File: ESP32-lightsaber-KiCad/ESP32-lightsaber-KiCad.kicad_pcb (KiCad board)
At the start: 2 copper layers, 7 parts, among them J1 Conn_01x05, SW1 SW_Push

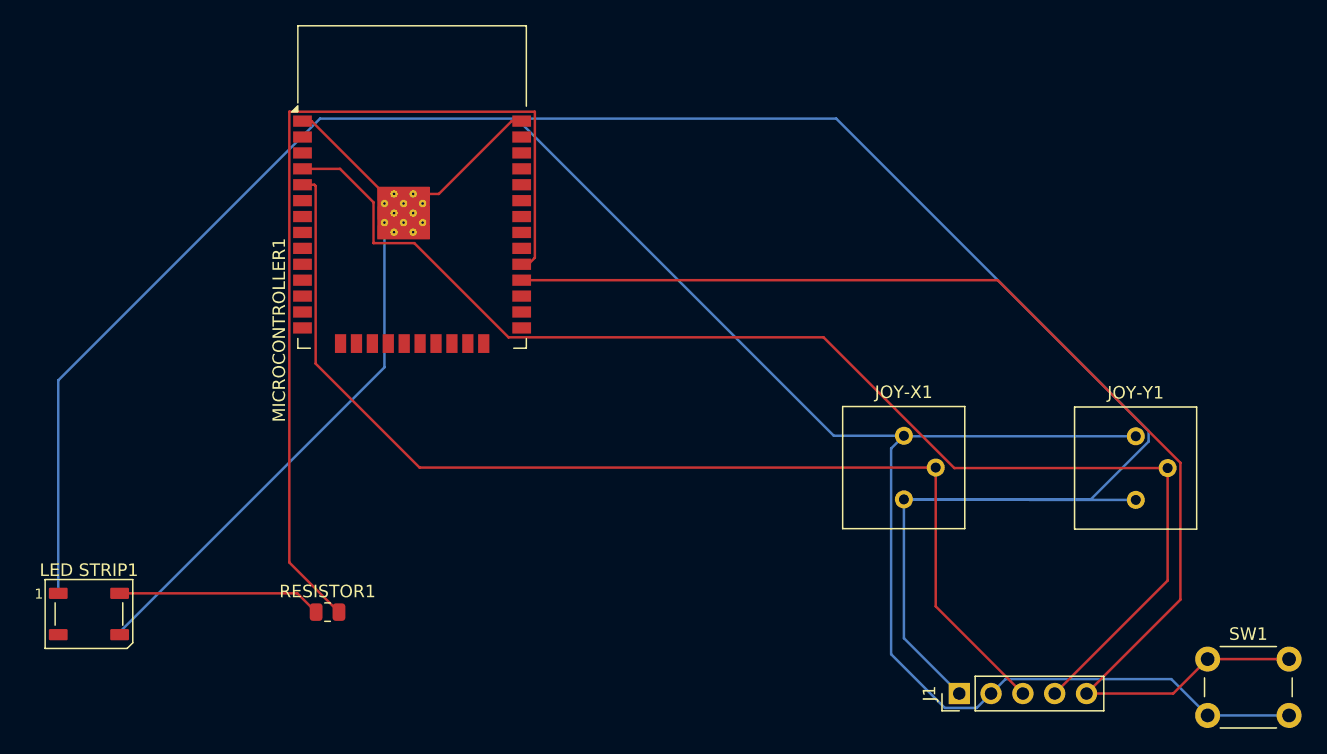
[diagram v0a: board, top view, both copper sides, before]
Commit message: Modified lightsaber schematic & PCB following prototype feedback
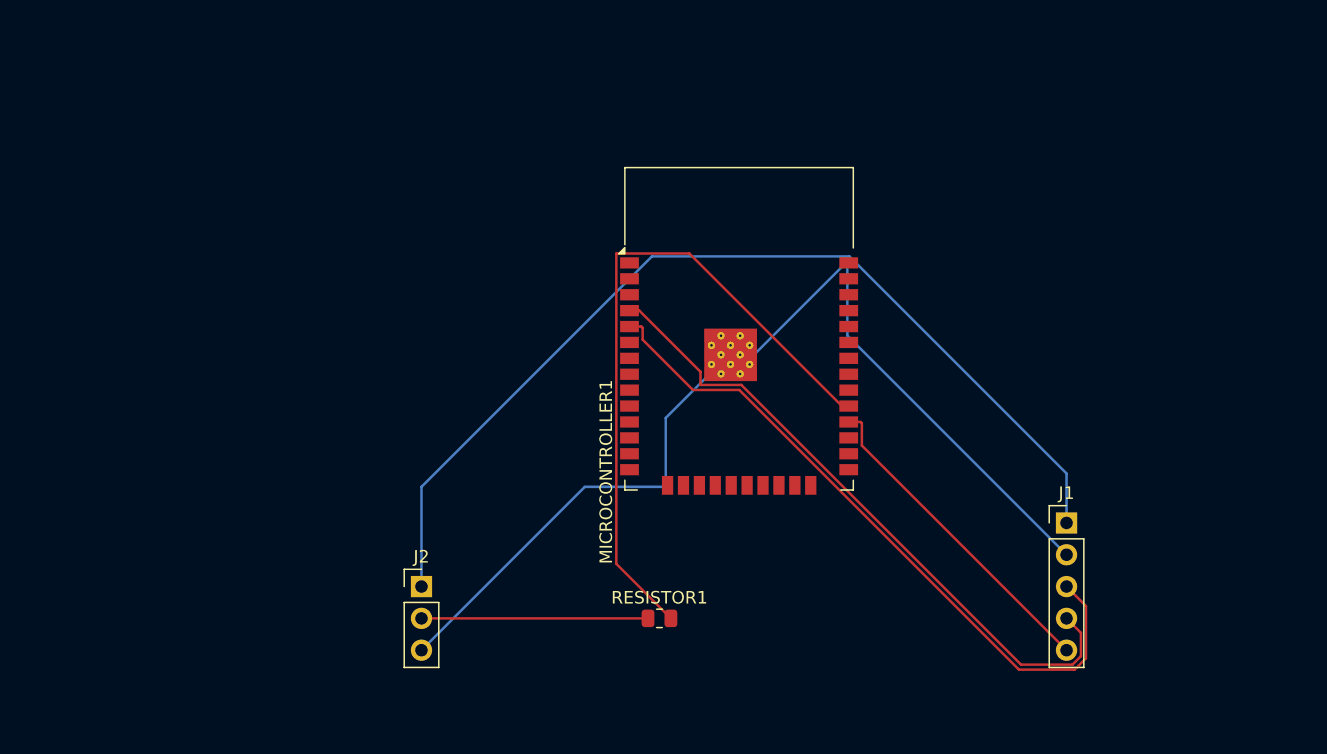
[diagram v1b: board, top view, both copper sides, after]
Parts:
- removed JOY-X1, JOY-Y1: R_Potentiometer, Potentiometer_THT:Potentiometer_Bourns_3386P_Vertical
- removed LED STRIP1: WS2812B, LED_SMD:LED_WS2812B_PLCC4_5.0x5.0mm_P3.2mm
- removed SW1: SW_Push, Button_Switch_THT:SW_PUSH_6mm_H9.5mm
- added J2: Conn_01x03, Connector_PinHeader_2.54mm:PinHeader_1x03_P2.54mm_Vertical, F.Cu at (95.0, 111.0)
- moved MICROCONTROLLER1 28.5 mm to (120.4, 93.4)
- moved RESISTOR1 26.5 mm to (114.0, 113.5)
- moved J1 16.1 mm to (146.5, 105.9), turned to 0 degrees
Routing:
- net +5V: track 181.2 -> 78.2 mm
- net GND: track 174.0 -> 80.7 mm
- net Net-(J1-Pin_5): track 97.5 -> 26.0 mm
- net Net-(J1-Pin_4): track 102.6 -> 52.1 mm
- net Net-(J1-Pin_3): track 89.1 -> 55.1 mm
- net Net-(MICROCONTROLLER1-IO5): track 74.1 -> 54.5 mm
- net Net-(J2-Pin_2): track 16.3 -> 18.1 mm

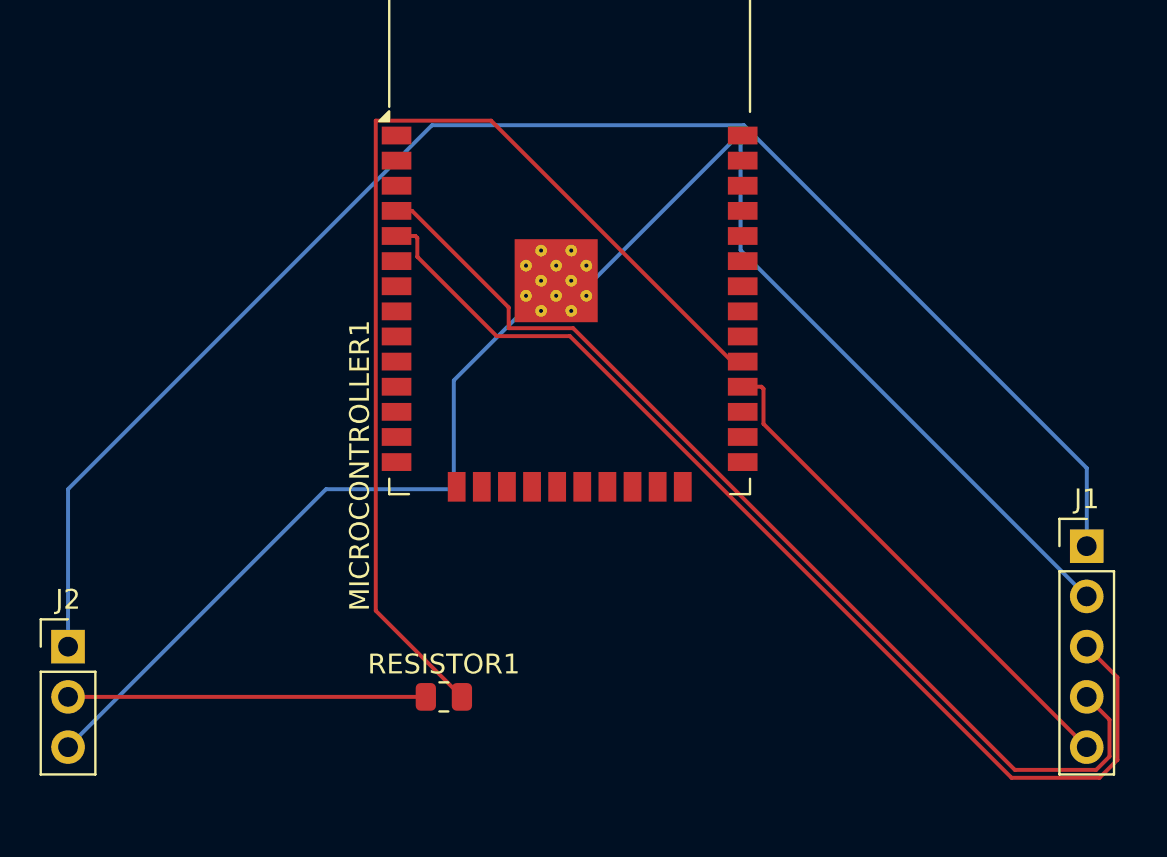
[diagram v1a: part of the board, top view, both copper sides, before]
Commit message: Thickened wires for 5V+ power & GND in PCB prototype for current flow
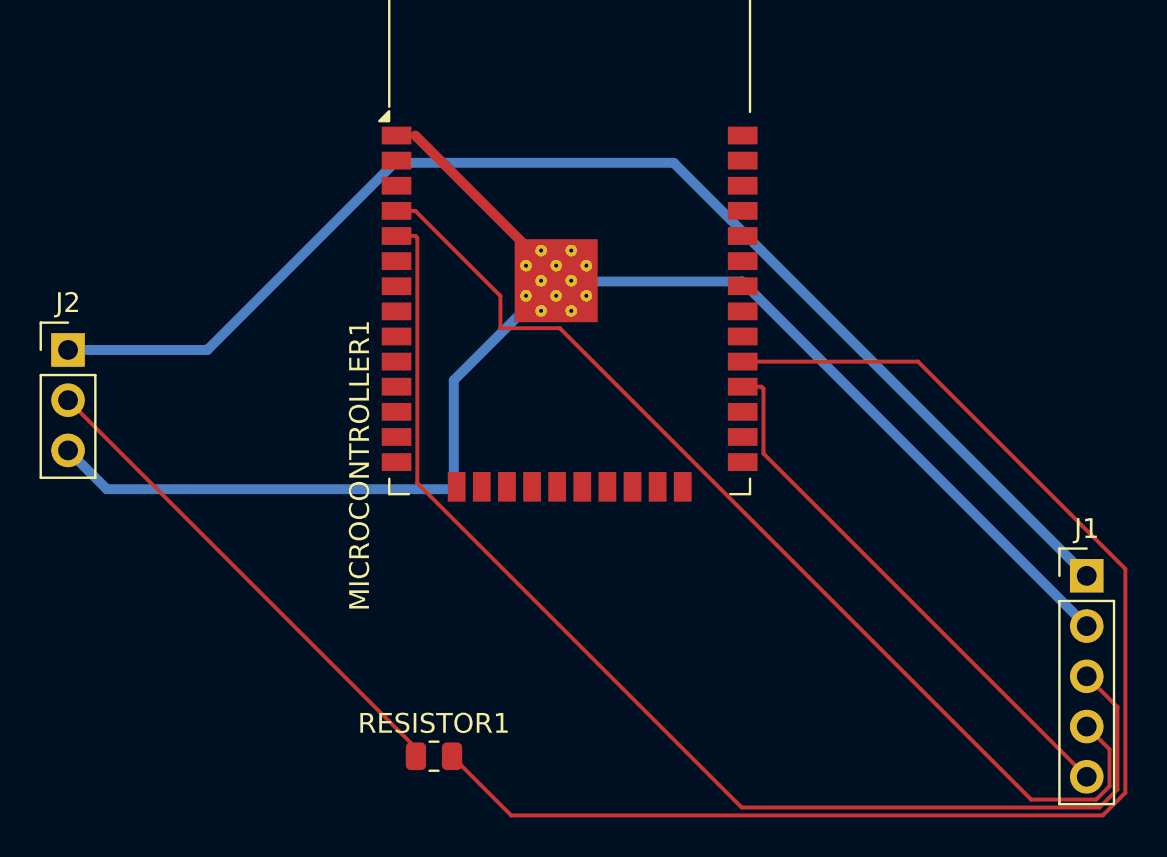
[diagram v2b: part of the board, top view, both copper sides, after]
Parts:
- moved J2 15.0 mm to (95.0, 96.0)
- moved RESISTOR1 3.04 mm to (113.5, 116.5)
- moved J1 1.50 mm to (146.5, 107.4)
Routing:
- net Net-(MICROCONTROLLER1-IO5): track 54.5 -> 70.8 mm
- net +5V: track 78.2 -> 64.1 mm
- net Net-(J1-Pin_3): track 55.1 -> 62.4 mm
- net Net-(J2-Pin_2): track 18.1 -> 25.3 mm
- net GND: track 80.7 -> 78.3 mm
- net Net-(J1-Pin_5): track 26.0 -> 27.5 mm
- net Net-(J1-Pin_4): track 52.1 -> 53.1 mm
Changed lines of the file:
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@@
 	(footprint "Connector_PinHeader_2.54mm:PinHeader_1x03_P2.54mm_Vertical"
 		(layer "F.Cu")
-		(at 95 110.96)
+		(at 95 95.96)
 		(descr "Through hole straight pin header, 1x03, 2.54mm pitch, single row")
 		(tags "Through hole pin header THT 1x03 2.54mm single row")
@@
 	(footprint "Resistor_SMD:R_0805_2012Metric"
 		(layer "F.Cu")
-		(at 114 113.5)
+		(at 113.5 116.5)
 		(descr "Resistor SMD 0805 (2012 Metric), square (rectangular) end terminal, IPC-7351 nominal, (Body size source: IPC-SM-782 page 72, https://www.pcb-3d.com/wordpress/wp-content/uploads/ipc-sm-782a_amendment_1_and_2.pdf), generated with kicad-footprint-generator")
 		(tags "resistor")
@@
 	(footprint "Connector_PinHeader_2.54mm:PinHeader_1x05_P2.54mm_Vertical"
 		(layer "F.Cu")
-		(at 146.5 105.88)
+		(at 146.5 107.38)
 		(descr "Through hole straight pin header, 1x05, 2.54mm pitch, single row")
 		(tags "Through hole pin header THT 1x05 2.54mm single row")
@@
 	)
 	(segment
-		(start 129 90.92)
-		(end 129 85)
-		(width 0.2)
+		(start 119.6775 92.24)
+		(end 119.6775 92.46)
+		(width 0.2)
+		(layer "F.Cu")
+		(net 1)
+	)
+	(segment
+		(start 111.6075 85.12)
+		(end 112.5575 85.12)
+		(width 0.2)
+		(layer "F.Cu")
+		(net 1)
+	)
+	(segment
+		(start 112.5575 85.12)
+		(end 119.6775 92.24)
+		(width 0.5)
+		(layer "F.Cu")
+		(net 1)
+	)
+	(segment
+		(start 96.96 103)
+		(end 95 101.04)
+		(width 0.5)
 		(layer "B.Cu")
 		(net 1)
 	)
 	(segment
-		(start 146.5 108.42)
-		(end 129 90.92)
-		(width 0.2)
+		(start 119.5 92.5)
+		(end 114.5 97.5)
+		(width 0.5)
 		(layer "B.Cu")
 		(net 1)
@@
 	(segment
 		(start 114.5 103)
-		(end 108.04 103)
-		(width 0.2)
+		(end 96.96 103)
+		(width 0.5)
 		(layer "B.Cu")
 		(net 1)
 	)
 	(segment
-		(start 129 85)
-		(end 121.5 92.5)
-		(width 0.2)
+		(start 129.08 92.5)
+		(end 119.5 92.5)
+		(width 0.5)
 		(layer "B.Cu")
 		(net 1)
 	)
 	(segment
-		(start 119.5 92.5)
-		(end 114.5 97.5)
-		(width 0.2)
+		(start 146.5 109.92)
+		(end 129.08 92.5)
+		(width 0.5)
 		(layer "B.Cu")
 		(net 1)
 	)
 	(segment
-		(start 108.04 103)
-		(end 95 116.04)
-		(width 0.2)
+		(start 114.5 97.5)
+		(end 114.5 103)
+		(width 0.5)
 		(layer "B.Cu")
 		(net 1)
 	)
 	(segment
-		(start 114.5 97.5)
-		(end 114.5 103)
-		(width 0.2)
-		(layer "B.Cu")
-		(net 1)
-	)
-	(segment
-		(start 121.5 92.5)
-		(end 119.5 92.5)
-		(width 0.2)
-		(layer "B.Cu")
-		(net 1)
-	)
-	(segment
-		(start 146.5 101.9329)
-		(end 146.5 105.88)
-		(width 0.2)
+		(start 111.5 86.5)
+		(end 125.62 86.5)
+		(width 0.5)
 		(layer "B.Cu")
 		(net 2)
 	)
 	(segment
-		(start 95 110.96)
-		(end 95 103)
-		(width 0.2)
+		(start 95 95.96)
+		(end 102.04 95.96)
+		(width 0.5)
 		(layer "B.Cu")
 		(net 2)
 	)
 	(segment
-		(start 113.401 84.599)
-		(end 129.1661 84.599)
-		(width 0.2)
+		(start 102.04 95.96)
+		(end 111.5 86.5)
+		(width 0.5)
 		(layer "B.Cu")
 		(net 2)
 	)
 	(segment
-		(start 95 103)
-		(end 113.401 84.599)
-		(width 0.2)
+		(start 125.62 86.5)
+		(end 146.5 107.38)
+		(width 0.5)
 		(layer "B.Cu")
 		(net 2)
 	)
 	(segment
-		(start 129.1661 84.599)
-		(end 146.5 101.9329)
-		(width 0.2)
-		(layer "B.Cu")
-		(net 2)
-	)
-	(segment
-		(start 114.9125 113.5)
-		(end 110.5565 109.144)
+		(start 137.972 96.55)
+		(end 129.1075 96.55)
 		(width 0.2)
 		(layer "F.Cu")
@@
 	)
 	(segment
-		(start 110.5565 84.369)
-		(end 116.3885 84.369)
+		(start 148.453 107.031)
+		(end 137.972 96.55)
 		(width 0.2)
 		(layer "F.Cu")
@@
 	)
 	(segment
-		(start 110.5565 109.144)
-		(end 110.5565 84.369)
+		(start 147.30896 119.493)
+		(end 148.453 118.34896)
 		(width 0.2)
 		(layer "F.Cu")
@@
 	)
 	(segment
-		(start 116.3885 84.369)
-		(end 128.5695 96.55)
+		(start 148.453 118.34896)
+		(end 148.453 107.031)
 		(width 0.2)
 		(layer "F.Cu")
@@
 	)
 	(segment
-		(start 128.5695 96.55)
-		(end 129.1075 96.55)
+		(start 117.4055 119.493)
+		(end 147.30896 119.493)
 		(width 0.2)
 		(layer "F.Cu")
@@
 	)
 	(segment
-		(start 120.5365 94.861)
-		(end 117.2765 94.861)
+		(start 114.4125 116.5)
+		(end 117.4055 119.493)
+		(width 0.2)
+		(layer "F.Cu")
+		(net 16)
+	)
+	(segment
+		(start 112.5575 88.93)
+		(end 111.6075 88.93)
 		(width 0.2)
 		(layer "F.Cu")
@@
 	)
 	(segment
-		(start 147.651 114.651)
-		(end 147.651 116.51676)
+		(start 116.861 93.2335)
+		(end 112.5575 88.93)
 		(width 0.2)
 		(layer "F.Cu")
@@
 	)
 	(segment
-		(start 142.8665 117.191)
-		(end 120.5365 94.861)
+		(start 143.691 118.691)
+		(end 119.861 94.861)
 		(width 0.2)
 		(layer "F.Cu")
@@
 	)
 	(segment
-		(start 112.3925 88.93)
-		(end 111.6075 88.93)
+		(start 147.651 118.01676)
+		(end 146.97676 118.691)
 		(width 0.2)
 		(layer "F.Cu")
@@
 	)
 	(segment
-		(start 146.97676 117.191)
-		(end 142.8665 117.191)
+		(start 119.861 94.861)
+		(end 116.861 94.861)
 		(width 0.2)
 		(layer "F.Cu")
@@
 	)
 	(segment
-		(start 117.2765 94.861)
-		(end 117.2765 93.814)
+		(start 146.5 115)
+		(end 147.651 116.151)
 		(width 0.2)
 		(layer "F.Cu")
@@
 	)
 	(segment
-		(start 117.2765 93.814)
-		(end 112.3925 88.93)
+		(start 146.97676 118.691)
+		(end 143.691 118.691)
 		(width 0.2)
 		(layer "F.Cu")
@@
 	)
 	(segment
-		(start 147.651 116.51676)
-		(end 146.97676 117.191)
+		(start 116.861 94.861)
+		(end 116.861 93.2335)
 		(width 0.2)
 		(layer "F.Cu")
@@
 	)
 	(segment
-		(start 146.5 113.5)
-		(end 147.651 114.651)
+		(start 147.651 116.151)
+		(end 147.651 118.01676)
 		(width 0.2)
 		(layer "F.Cu")
 		(net 26)
-	)
-	(segment
-		(start 146.5 116.04)
-		(end 130.1585 99.6985)
-		(width 0.2)
-		(layer "F.Cu")
-		(net 27)
-	)
-	(segment
-		(start 130.1585 99.6985)
-		(end 130.1585 97.921)
-		(width 0.2)
-		(layer "F.Cu")
-		(net 27)
 	)
 	(segment
@@
 	)
 	(segment
+		(start 146.5 117.54)
+		(end 130.1585 101.1985)
+		(width 0.2)
+		(layer "F.Cu")
+		(net 27)
+	)
+	(segment
+		(start 130.1585 101.1985)
+		(end 130.1585 97.921)
+		(width 0.2)
+		(layer "F.Cu")
+		(net 27)
+	)
+	(segment
 		(start 130.1585 97.921)
 		(end 130.0575 97.82)
@@
 	)
 	(segment
-		(start 116.6695 95.262)
-		(end 112.6585 91.251)
+		(start 129.0575 119.092)
+		(end 112.6585 102.693)
 		(width 0.2)
 		(layer "F.Cu")
@@
 	)
 	(segment
-		(start 142.7004 117.592)
-		(end 120.3704 95.262)
+		(start 112.6585 90.301)
+		(end 112.5575 90.2)
 		(width 0.2)
 		(layer "F.Cu")
@@
 	)
 	(segment
-		(start 148.052 112.512)
-		(end 148.052 116.68286)
+		(start 148.052 118.18286)
+		(end 147.14286 119.092)
 		(width 0.2)
 		(layer "F.Cu")
@@
 	)
 	(segment
-		(start 120.3704 95.262)
-		(end 116.6695 95.262)
-		(width 0.2)
-		(layer "F.Cu")
-		(net 29)
-	)
-	(segment
-		(start 148.052 116.68286)
-		(end 147.14286 117.592)
-		(width 0.2)
-		(layer "F.Cu")
-		(net 29)
-	)
-	(segment
-		(start 112.6585 91.251)
+		(start 112.6585 102.693)
 		(end 112.6585 90.301)
-		(width 0.2)
-		(layer "F.Cu")
-		(net 29)
-	)
-	(segment
-		(start 147.14286 117.592)
-		(end 142.7004 117.592)
-		(width 0.2)
-		(layer "F.Cu")
-		(net 29)
-	)
-	(segment
-		(start 146.5 110.96)
-		(end 148.052 112.512)
 		(width 0.2)
 		(layer "F.Cu")
@@
 	)
 	(segment
-		(start 112.6585 90.301)
-		(end 112.5575 90.2)
+		(start 147.14286 119.092)
+		(end 129.0575 119.092)
 		(width 0.2)
 		(layer "F.Cu")
@@
 	)
 	(segment
-		(start 95 113.5)
-		(end 113.0875 113.5)
-		(width 0.2)
-		(layer "F.Cu")
+		(start 148.052 114.012)
+		(end 148.052 118.18286)
+		(width 0.2)
+		(layer "F.Cu")
+		(net 29)
+	)
+	(segment
+		(start 146.5 112.46)
+		(end 148.052 114.012)
+		(width 0.2)
+		(layer "F.Cu")
+		(net 29)
+	)
+	(segment
+		(start 112.5875 116.5)
+		(end 112.5875 116.0875)
+		(width 0.2)
+		(layer "F.Cu")
+		(net 37)
+	)
+	(segment
+		(start 112.5875 116.0875)
+		(end 95 98.5)
+		(width 0.2)
+		(layer "F.Cu")
